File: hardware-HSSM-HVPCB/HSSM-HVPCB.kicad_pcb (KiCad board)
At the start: 2 copper layers, 42 x 36 mm, 64 parts, among them J1 2601-1108, K1 G6DN-1A-L DC12, K2 G6DN-1A-L DC12, Q1 Q_NMOS_SOT-23_IRLML6344, Q2 Q_NMOS_SOT-23_IRLML6344, U1 LNK3204D-TL, U2 CS5480-INZ, U3 LTV-354T, U4 LTV-354T, U6 TPS560200DBVR_SOIC_6_TI

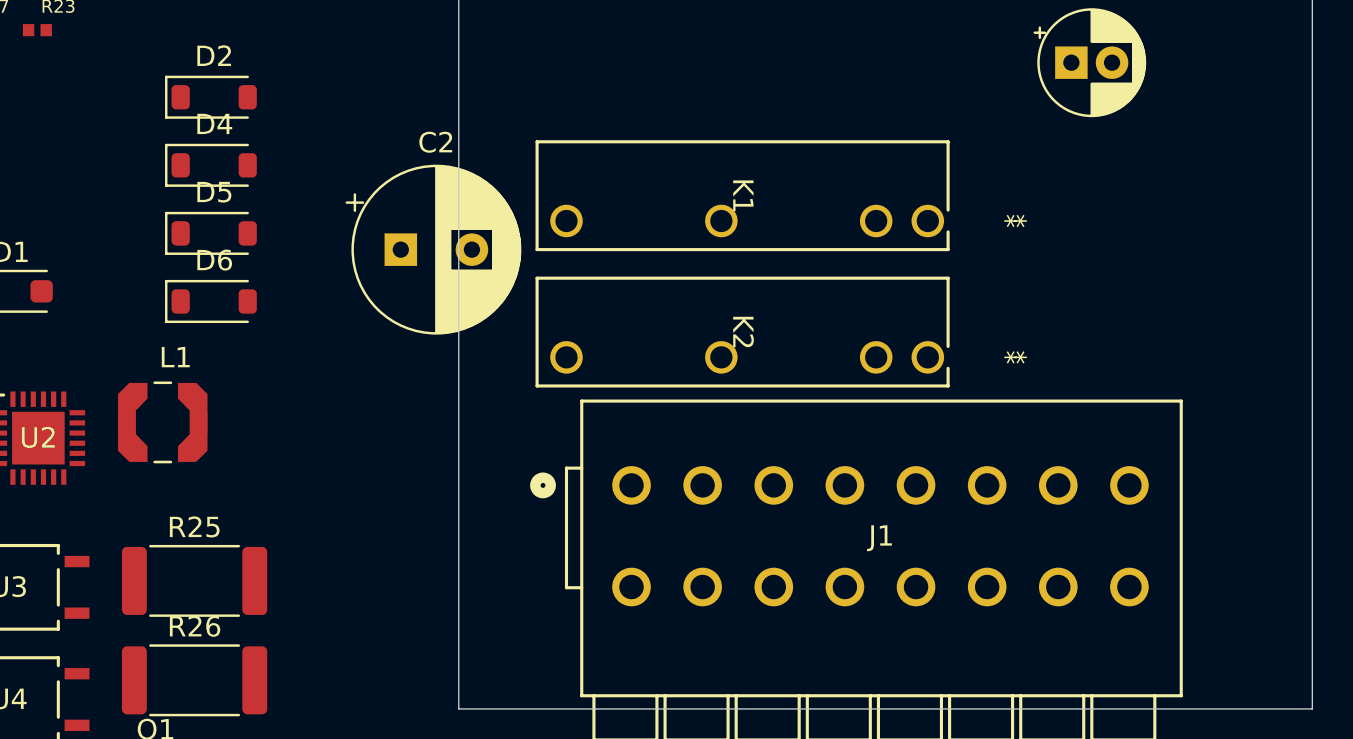
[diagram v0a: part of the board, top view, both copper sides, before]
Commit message: [#7] Components placement WIP
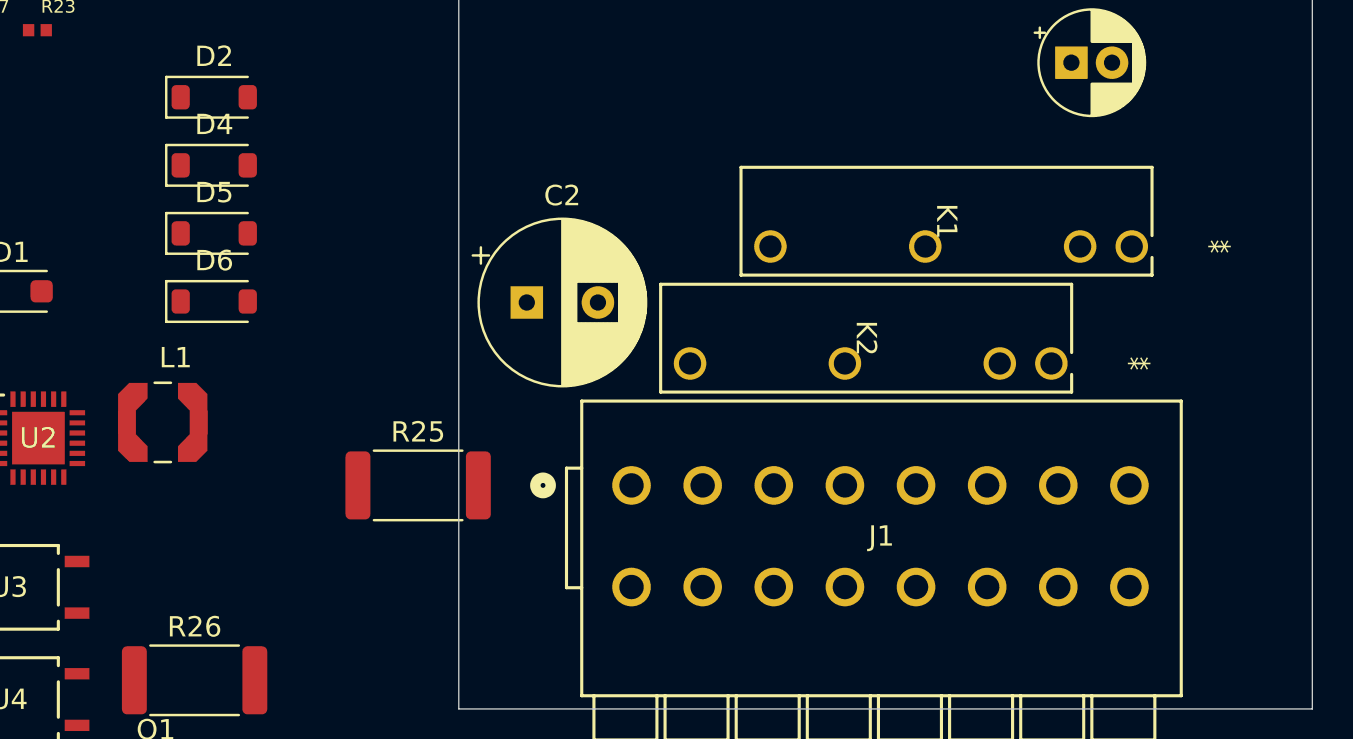
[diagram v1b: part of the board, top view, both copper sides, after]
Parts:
- moved R25 12.0 mm to (130.0, 119.0)
- moved K1 10.1 mm to (165.1, 107.2)
- moved C2 6.72 mm to (135.3, 110.0)
- moved K2 6.09 mm to (161.2, 113.0)
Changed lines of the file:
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@@
 	(footprint "HSSM-HVPCB:RELAY_G6DN-1A_OMR"
 		(layer "F.Cu")
-		(at 155.080001 112.7 -90)
+		(at 161.16 113 -90)
 		(tags "G6DN-1A-L DC12 ")
 		(property "Reference" "K2"
@@
 	(footprint "HSSM-HVPCB:860021374009"
 		(layer "F.Cu")
-		(at 129.147349 107.4)
+		(at 135.347349 110)
 		(descr "CP, Radial series, Radial, pin pitch=3.50mm, , diameter=8mm, Electrolytic Capacitor")
 		(tags "CP Radial series Radial pin pitch 3.50mm  diameter 8mm Electrolytic Capacitor")
@@
 	(footprint "HSSM-HVPCB:R_2512"
 		(layer "F.Cu")
-		(at 119 123.7)
+		(at 130 119)
 		(descr "Resistor SMD 2512 (6332 Metric), square (rectangular) end terminal, IPC_7351 nominal, (Body size source: IPC-SM-782 page 72, https://www.pcb-3d.com/wordpress/wp-content/uploads/ipc-sm-782a_amendment_1_and_2.pdf), generated with kicad-footprint-generator")
 		(tags "resistor")
@@
 	(footprint "HSSM-HVPCB:RELAY_G6DN-1A_OMR"
 		(layer "F.Cu")
-		(at 155.08 105.9896 -90)
+		(at 165.115001 107.244999 -90)
 		(tags "G6DN-1A-L DC12 ")
 		(property "Reference" "K1"

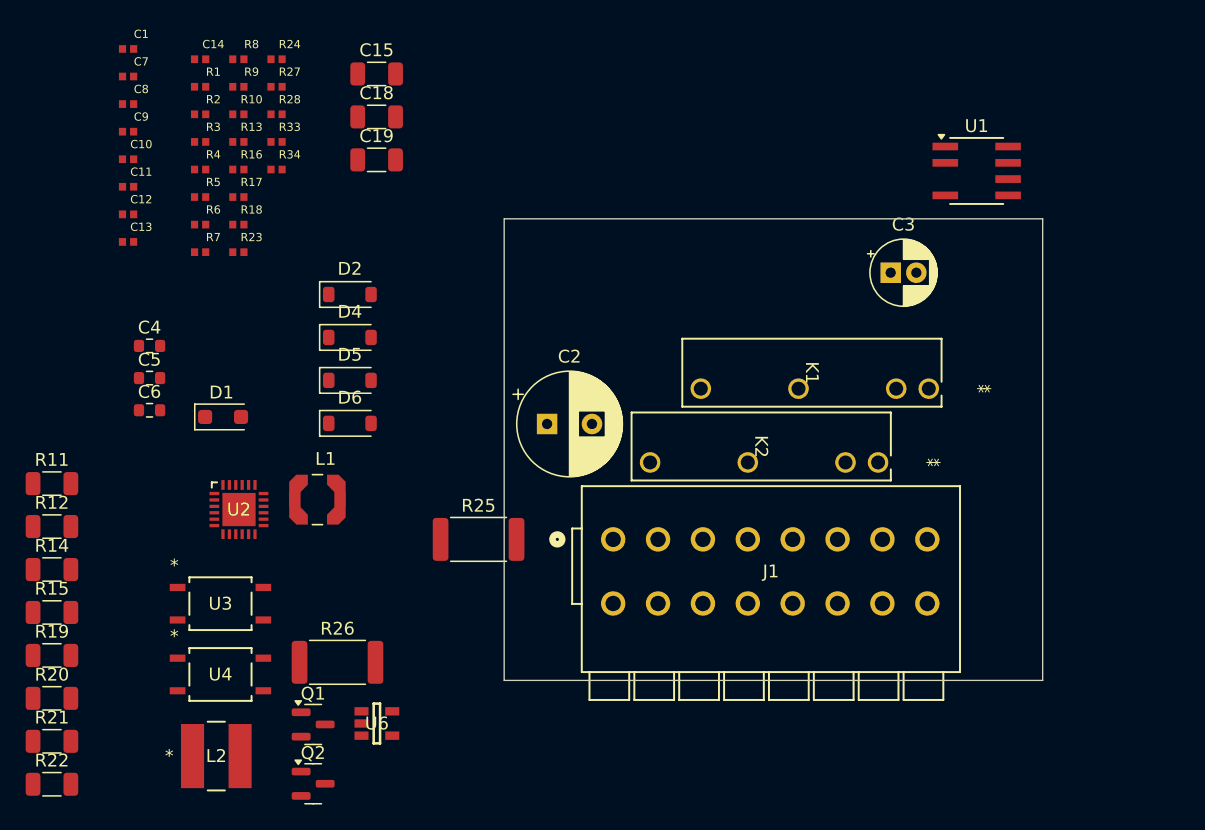
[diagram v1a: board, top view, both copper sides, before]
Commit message: [#7] Components placement WIP
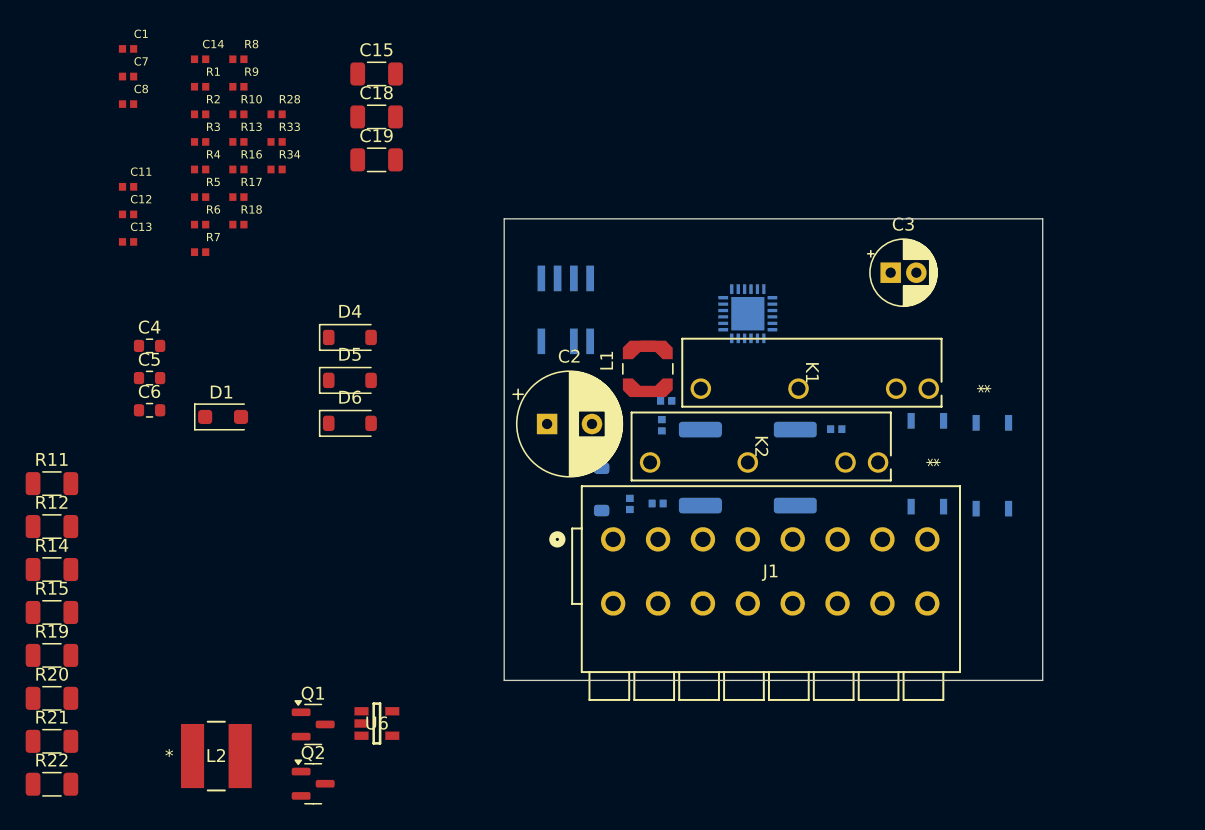
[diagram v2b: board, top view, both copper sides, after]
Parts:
- C10, C9, D2, R23, R24, R25, R26, R27, U1, U2, U3, U4: moved to B.Cu
- moved U3 61.2 mm to (170.1, 113.3), turned to 90 degrees
- moved U4 57.5 mm to (165.0, 113.1), turned to 90 degrees
- moved R27 51.2 mm to (157.9, 110.4), turned to 180 degrees
- moved C9 47.5 mm to (144.3, 110.1), turned to 90 degrees
- moved C10 47.5 mm to (141.8, 116.2), turned to 90 degrees
- moved U2 42.5 mm to (151.0, 101.4), turned to 180 degrees
- moved R24 40.4 mm to (144.6, 108.2)
- moved R26 38.8 mm to (154.7, 113.4), turned to 90 degrees
- moved R23 38.1 mm to (144.0, 116.2), turned to 180 degrees
- moved U1 33.8 mm to (136.8, 101.1), turned to 90 degrees
- moved L1 27.7 mm to (143.2, 105.7), turned to 90 degrees
- moved D2 24.8 mm to (139.6, 115.1), turned to -90 degrees
- moved R25 18.2 mm to (147.3, 113.4), turned to 90 degrees

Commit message: [#7] Components placement WIP
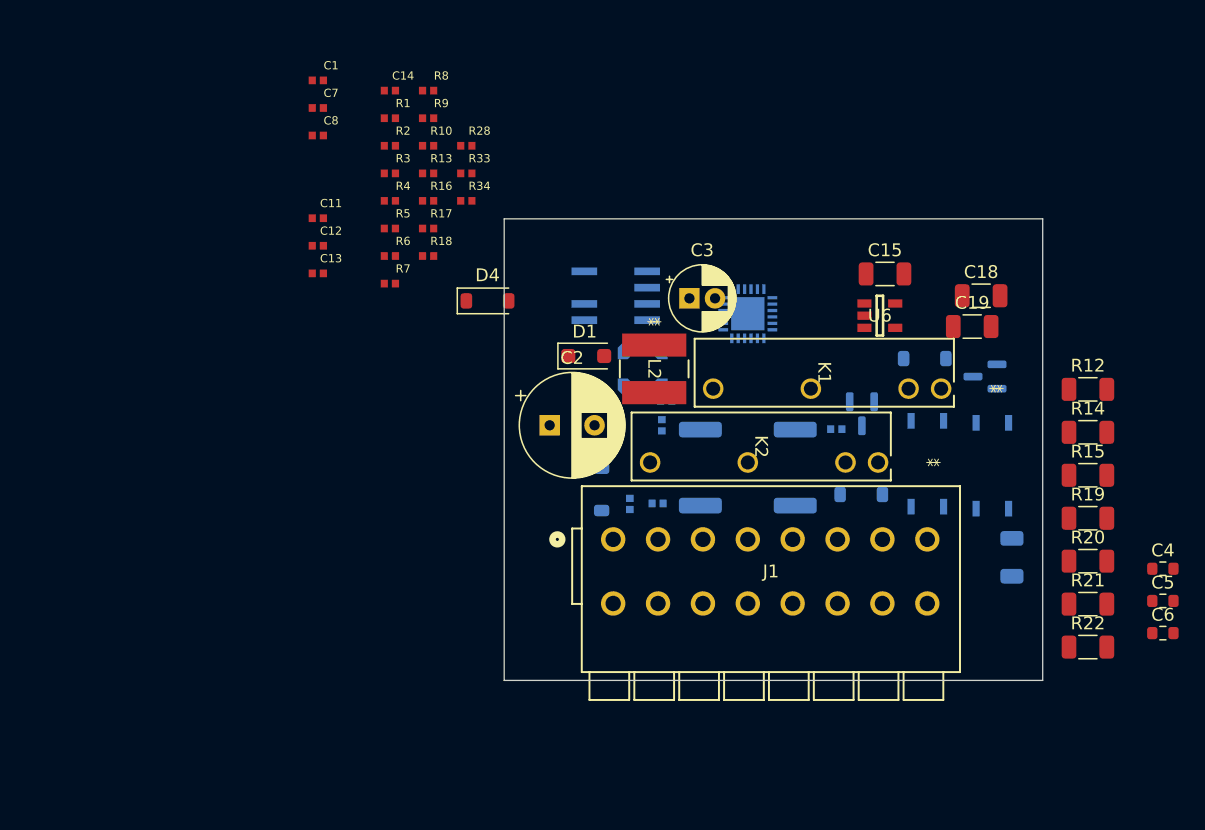
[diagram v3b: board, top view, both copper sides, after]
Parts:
- D5, D6, L1, Q1, Q2, R11: moved to B.Cu
- moved R19 81.5 mm to (177.5, 117.3)
- moved R12 81.5 mm to (177.5, 107.3)
- moved R14 81.5 mm to (177.5, 110.7)
- moved R15 81.5 mm to (177.5, 114.0)
- moved R20 81.5 mm to (177.5, 120.7)
- moved R21 81.5 mm to (177.5, 124.0)
- moved R22 81.5 mm to (177.5, 127.4)
- moved C4 80.9 mm to (183.4, 121.3)
- moved C5 80.9 mm to (183.4, 123.8)
- moved C6 80.9 mm to (183.4, 126.3)
- moved R11 75.1 mm to (171.6, 120.4), turned to 90 degrees
- moved Q1 59.0 mm to (169.5, 106.3), turned to 180 degrees
- moved Q2 51.6 mm to (159.9, 109.2), turned to -90 degrees
- moved U6 50.5 mm to (161.3, 101.6)
- moved C18 49.2 mm to (169.2, 100.0)
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
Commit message: [#7] Components placement WIP
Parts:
- R12, R14, R15, R18, R19, R20, R21, R22: moved to B.Cu
- moved R18 29.6 mm to (155.1, 102.8), turned to 180 degrees
- moved R19 27.9 mm to (151.8, 106.6), turned to 90 degrees
- moved R15 22.5 mm to (159.8, 127.9), turned to 180 degrees
- moved R14 21.4 mm to (164.8, 127.9), turned to 180 degrees
- moved R12 18.5 mm to (171.5, 124.8), turned to 90 degrees
- moved U4 15.5 mm to (154.6, 124.6)
- moved R20 2.50 mm to (177.4, 118.2), turned to 180 degrees
- moved R11 0.41 mm to (171.5, 120.0)
- turned R21 to 180 degrees
- turned R22 to 180 degrees

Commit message: [#6] Replace crystal oscillator
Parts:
- added Y1: OSC_2520_4.096MHz_25ppm_ECS-2520MVLC-041-BN-TR, HSSM-HVPCB:ECS-2520MVLC-041-BN-TR, B.Cu at (155.3, 97.0)

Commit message: [#6] Remove status LEDs from HVPCB
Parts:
- removed R10, R9: R_220R_1pct_0402_RC0402FR-07220RL, HSSM-HVPCB:R_0402
- moved Y1 2.22 mm to (156.0, 99.1)

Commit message: [#6] Add L 3012
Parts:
- added L4: L_10uH_20pct_1A_SDCL1V3012-100M-R, HSSM-HVPCB:L_3012, F.Cu at (142.2, 89.2)

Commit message: [#3] Remove fuses
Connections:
- K1 pad 5: Net-(F4-Pad2) -> AC_Q1
- K2 pad 5: Net-(F3-Pad2) -> AC_Q2
